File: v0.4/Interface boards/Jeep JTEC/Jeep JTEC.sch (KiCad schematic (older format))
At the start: 6 parts, among them J1 Conn_02x20_Counter_Clockwise

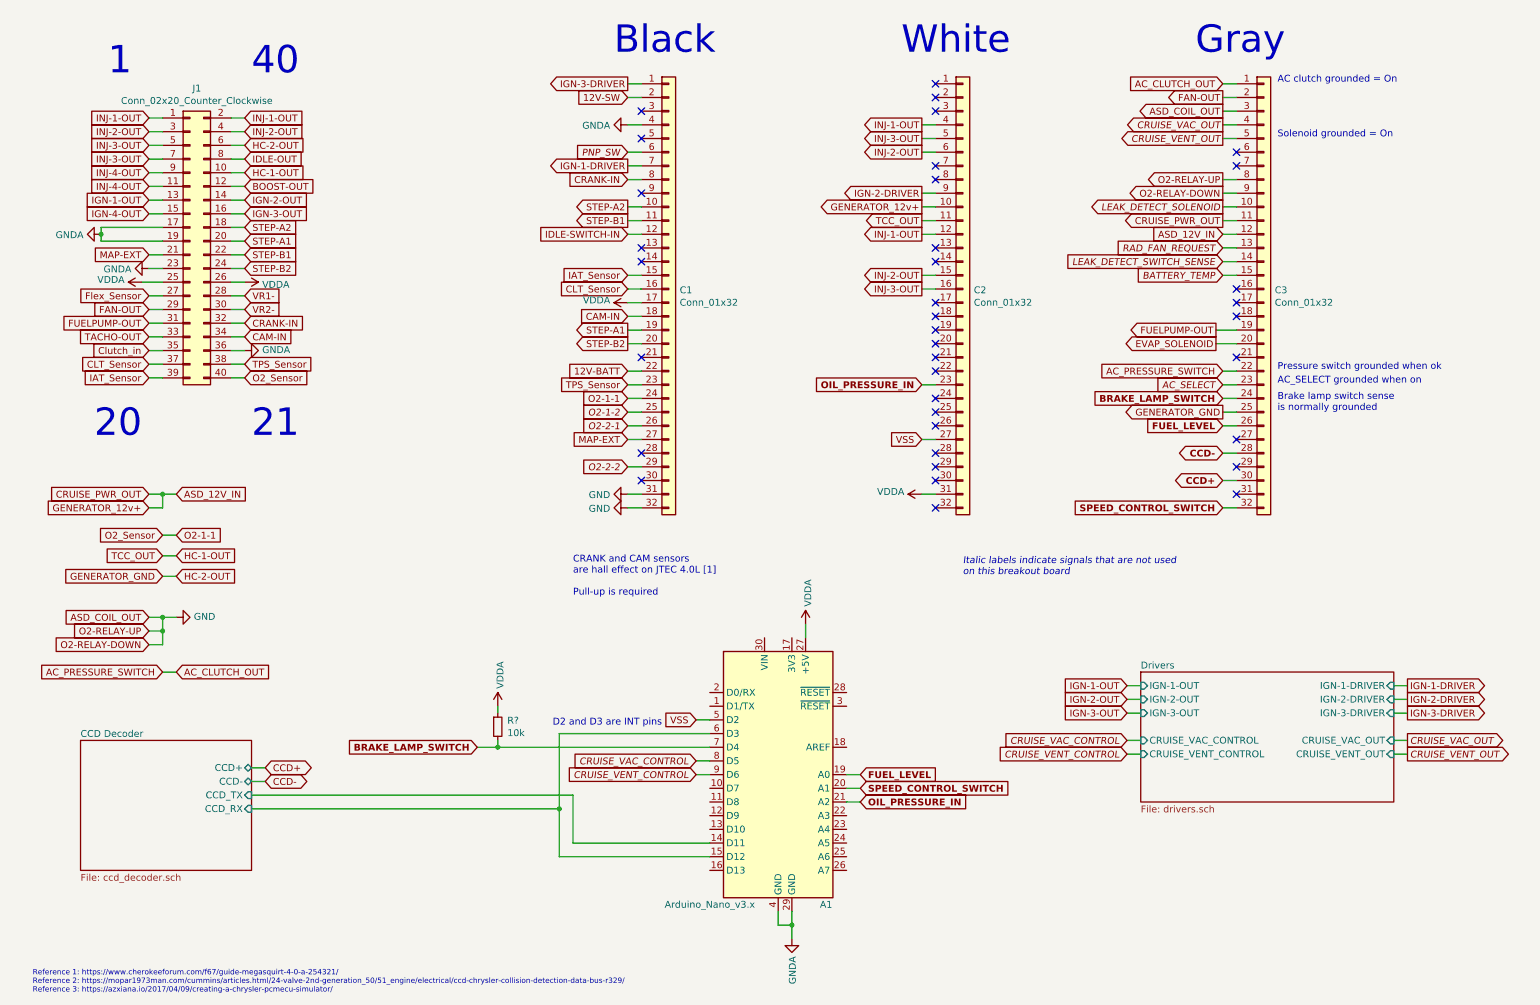
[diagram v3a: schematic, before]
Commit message: Add voltage sense circuit for alternator control
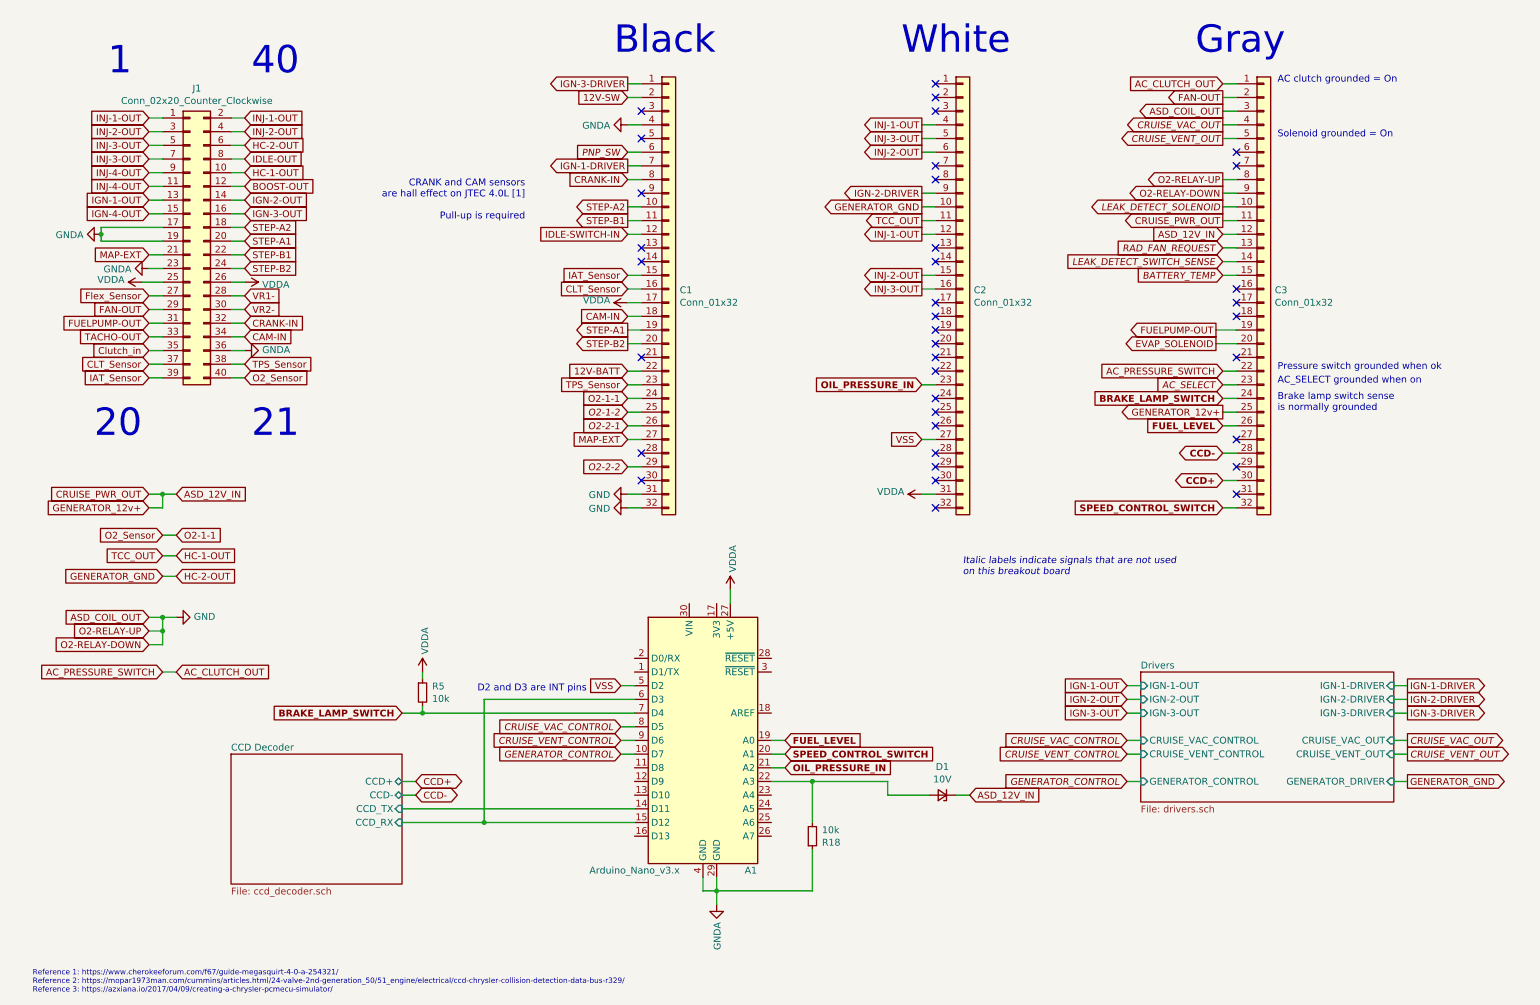
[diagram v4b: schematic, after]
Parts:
- added D1: 10V, Package_TO_SOT_SMD:SOT-23, symbol Misc:D_Zener_SOT-23
- added R18: 10k, Resistor_SMD:R_0805_2012Metric, symbol Device:R_Small
- R5: renamed from R?; footprint (none) -> Resistor_SMD:R_0805_2012Metric
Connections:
- net ASD_12V_IN: now also C3.25 (Pin_25), D1.3 (K); no longer C2.10 (Pin_10)
- net GENERATOR_GND: now also C2.10 (Pin_10); no longer C3.25 (Pin_25)
- net GNDA: now also R18.1
- net GENERATOR_CONTROL: now reaches A1.10 (D7)
- net at A1.22 (A3): now also D1.1 (A), R18.2
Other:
- moved on the sheet: A1, R5
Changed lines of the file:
@@
 Wire Wire Line
 	5000 1700 4900 1700
-Text Notes 4500 4750 0    50   ~ 0
+Text Notes 4150 2000 2    50   ~ 0
 CRANK and CAM sensors\nare hall effect on JTEC 4.0L [1]\n\nPull-up is required
 Text Notes 550  7650 0    39   ~ 0
@@
 Text GLabel 1600 4000 2    50   Input ~ 0
 ASD_12V_IN
-Text GLabel 7050 1900 0    50   Output ~ 0
+Text GLabel 9250 3400 0    50   Output ~ 0
 GENERATOR_12v+
 Wire Wire Line
@@
 Wire Wire Line
 	1400 5100 1500 5100
-Text GLabel 9250 3400 0    50   Output ~ 0
+Text GLabel 7050 1900 0    50   Output ~ 0
 GENERATOR_GND
 Wire Wire Line
@@
 L MCU_Module:Arduino_Nano_v3.x A1
 U 1 1 6153DDCF
-P 6000 6050
-F 0 "A1" H 6350 5100 50  0000 C CNN
-F 1 "Arduino_Nano_v3.x" H 5500 5100 50  0000 C CNN
-F 2 "Module:Arduino_Nano" H 6000 6050 50  0001 C CIN
-F 3 "http://www.mouser.com/pdfdocs/Gravitech_Arduino_Nano3_0.pdf" H 6000 6050 50  0001 C CNN
-	1    6000 6050
+P 5450 5800
+F 0 "A1" H 5800 4850 50  0000 C CNN
+F 1 "Arduino_Nano_v3.x" H 4950 4850 50  0000 C CNN
+F 2 "Module:Arduino_Nano" H 5450 5800 50  0001 C CIN
+F 3 "http://www.mouser.com/pdfdocs/Gravitech_Arduino_Nano3_0.pdf" H 5450 5800 50  0001 C CNN
+	1    5450 5800
 	1    0    0    -1
 $EndComp
-$Sheet
-S 900  5800 1250 950
-U 615FCF77
-F0 "CCD Decoder" 50
-F1 "ccd_decoder.sch" 50
-F2 "CCD-" B R 2150 6100 50
-F3 "CCD+" B R 2150 6000 50
-F4 "CCD_TX" I R 2150 6200 50
-F5 "CCD_RX" I R 2150 6300 50
-$EndSheet
-Wire Wire Line
-	5500 5750 4400 5750
-Wire Wire Line
-	4400 5750 4400 6300
-Wire Wire Line
-	4400 6300 2150 6300
-Wire Wire Line
-	5500 6650 4400 6650
-Wire Wire Line
-	5500 6550 4500 6550
-Wire Wire Line
-	4500 6550 4500 6200
-Wire Wire Line
-	4500 6200 2150 6200
+Wire Wire Line
+	4950 5500 3850 5500
+Wire Wire Line
+	4950 6400 3850 6400
 Text GLabel 9250 3700 0    50   BiDi ~ 10
 CCD-
 Text GLabel 9250 3900 0    50   BiDi ~ 10
 CCD+
-Text GLabel 2250 6000 2    50   BiDi ~ 0
-CCD+
-Wire Wire Line
-	2250 6000 2150 6000
-Text GLabel 2250 6100 2    50   BiDi ~ 0
-CCD-
-Wire Wire Line
-	2150 6100 2250 6100
-Wire Wire Line
-	4400 6300 4400 6650
-Connection ~ 4400 6300
 Text GLabel 9250 3500 0    50   Input ~ 10
 FUEL_LEVEL
-Text GLabel 6600 6050 2    50   Input ~ 10
+Text GLabel 6050 5800 2    50   Input ~ 10
 FUEL_LEVEL
 Wire Wire Line
-	6500 6050 6600 6050
-$Comp
-L power:VDDA #PWR?
+	5950 5800 6050 5800
+$Comp
+L power:VDDA #PWR017
 U 1 1 61616827
-P 6200 4950
-F 0 "#PWR?" H 6200 4800 50  0001 C CNN
-F 1 "VDDA" V 6218 5078 50  0000 L CNN
-F 2 "" H 6200 4950 50  0001 C CNN
-F 3 "" H 6200 4950 50  0001 C CNN
-	1    6200 4950
+P 5650 4700
+F 0 "#PWR017" H 5650 4550 50  0001 C CNN
+F 1 "VDDA" V 5668 4828 50  0000 L CNN
+F 2 "" H 5650 4700 50  0001 C CNN
+F 3 "" H 5650 4700 50  0001 C CNN
+	1    5650 4700
 	1    0    0    -1
 $EndComp
 Wire Wire Line
-	6200 5050 6200 4950
-$Comp
-L power:GNDA #PWR?
+	5650 4800 5650 4700
+$Comp
+L power:GNDA #PWR016
 U 1 1 6161D4CA
-P 6100 7250
-F 0 "#PWR?" H 6100 7000 50  0001 C CNN
-F 1 "GNDA" V 6105 7122 50  0000 R CNN
-F 2 "" H 6100 7250 50  0001 C CNN
-F 3 "" H 6100 7250 50  0001 C CNN
-	1    6100 7250
+P 5550 7000
+F 0 "#PWR016" H 5550 6750 50  0001 C CNN
+F 1 "GNDA" V 5555 6872 50  0000 R CNN
+F 2 "" H 5550 7000 50  0001 C CNN
+F 3 "" H 5550 7000 50  0001 C CNN
+	1    5550 7000
 	1    0    0    -1
 $EndComp
 Wire Wire Line
-	6100 7150 6100 7050
-Wire Wire Line
-	6100 7150 6000 7150
-Wire Wire Line
-	6000 7150 6000 7050
-Connection ~ 6100 7150
-Wire Wire Line
-	6100 7250 6100 7150
-Wire Wire Line
-	6600 6150 6500 6150
+	5550 6900 5550 6800
+Wire Wire Line
+	5550 6900 5450 6900
+Wire Wire Line
+	5450 6900 5450 6800
+Connection ~ 5550 6900
+Wire Wire Line
+	5550 7000 5550 6900
+Wire Wire Line
+	6050 5900 5950 5900
 Text GLabel 9250 4100 0    50   Input ~ 10
 SPEED_CONTROL_SWITCH
-Text GLabel 6600 6150 2    50   Input ~ 10
+Text GLabel 6050 5900 2    50   Input ~ 10
 SPEED_CONTROL_SWITCH
 Text GLabel 7050 3200 0    50   Input ~ 10
 OIL_PRESSURE_IN
-Text GLabel 6600 6250 2    50   Input ~ 10
+Text GLabel 6050 6000 2    50   Input ~ 10
 OIL_PRESSURE_IN
 Wire Wire Line
-	6600 6250 6500 6250
+	6050 6000 5950 6000
 Text GLabel 7050 3600 0    50   Input ~ 0
 VSS
-Text GLabel 5400 5650 0    50   Input ~ 0
+Text GLabel 4850 5400 0    50   Input ~ 0
 VSS
 Wire Wire Line
-	5400 5650 5500 5650
-Text Notes 5150 5700 2    50   ~ 0
+	4850 5400 4950 5400
+Text Notes 4600 5450 2    50   ~ 0
 D2 and D3 are INT pins
 Text GLabel 7050 1300 0    50   Output ~ 0
@@
 Text GLabel 9250 3300 0    50   Input ~ 10
 BRAKE_LAMP_SWITCH
-Text GLabel 3800 5850 0    50   Input ~ 10
+Text GLabel 3250 5600 0    50   Input ~ 10
 BRAKE_LAMP_SWITCH
 $Comp
 L Device:R_Small R?
 U 1 1 6173A1FE
-P 3950 5700
+P 3400 5450
 AR Path="/615FCF77/6173A1FE" Ref="R?"  Part="1"
-AR Path="/6173A1FE" Ref="R?"  Part="1"
-F 0 "R?" H 4020 5746 50  0000 L CNN
-F 1 "10k" H 4020 5655 50  0000 L CNN
-F 2 "" V 3880 5700 50  0001 C CNN
-F 3 "~" H 3950 5700 50  0001 C CNN
-	1    3950 5700
+AR Path="/6173A1FE" Ref="R5"  Part="1"
+F 0 "R5" H 3470 5496 50  0000 L CNN
+F 1 "10k" H 3470 5405 50  0000 L CNN
+F 2 "Resistor_SMD:R_0805_2012Metric" V 3330 5450 50  0001 C CNN
+F 3 "~" H 3400 5450 50  0001 C CNN
+	1    3400 5450
 	1    0    0    -1
 $EndComp
 Wire Wire Line
-	3950 5550 3950 5600
-Wire Wire Line
-	3950 5800 3950 5850
-Wire Wire Line
-	5500 5850 3950 5850
-Connection ~ 3950 5850
-Wire Wire Line
-	3950 5850 3800 5850
-$Comp
-L power:VDDA #PWR?
+	3400 5300 3400 5350
+Wire Wire Line
+	3400 5550 3400 5600
+Wire Wire Line
+	4950 5600 3400 5600
+Connection ~ 3400 5600
+Wire Wire Line
+	3400 5600 3250 5600
+$Comp
+L power:VDDA #PWR015
 U 1 1 617EB87A
-P 3950 5550
-F 0 "#PWR?" H 3950 5400 50  0001 C CNN
-F 1 "VDDA" V 3968 5678 50  0000 L CNN
-F 2 "" H 3950 5550 50  0001 C CNN
-F 3 "" H 3950 5550 50  0001 C CNN
-	1    3950 5550
+P 3400 5300
+F 0 "#PWR015" H 3400 5150 50  0001 C CNN
+F 1 "VDDA" V 3418 5428 50  0000 L CNN
+F 2 "" H 3400 5300 50  0001 C CNN
+F 3 "" H 3400 5300 50  0001 C CNN
+	1    3400 5300
 	1    0    0    -1
 $EndComp
@@
 Wire Wire Line
 	10600 5900 10500 5900
-Text GLabel 5400 5950 0    50   Input Italic 0
+Text GLabel 4850 5700 0    50   Input Italic 0
 CRUISE_VAC_CONTROL
 Wire Wire Line
-	5400 5950 5500 5950
-Text GLabel 5400 6050 0    50   Input Italic 0
+	4850 5700 4950 5700
+Text GLabel 4850 5800 0    50   Input Italic 0
 CRUISE_VENT_CONTROL
 Wire Wire Line
-	5400 6050 5500 6050
+	4850 5800 4950 5800
 Text GLabel 8550 5800 0    50   Input Italic 0
 CRUISE_VAC_CONTROL
@@
 F10 "CRUISE_VENT_CONTROL" I L 8650 5900 50
 F11 "CRUISE_VENT_OUT" I R 10500 5900 50
+F12 "GENERATOR_CONTROL" I L 8650 6100 50
+F13 "GENERATOR_DRIVER" I R 10500 6100 50
 $EndSheet
+Text GLabel 10600 6100 2    50   Output ~ 0
+GENERATOR_GND
+Wire Wire Line
+	10600 6100 10500 6100
+Text GLabel 4850 5900 0    50   Input Italic 0
+GENERATOR_CONTROL
+Wire Wire Line
+	4850 5900 4950 5900
+Text GLabel 8550 6100 0    50   Input Italic 0
+GENERATOR_CONTROL
+Wire Wire Line
+	8550 6100 8650 6100
+$Comp
+L Device:R_Small R?
+U 1 1 618ADDF1
+P 6250 6500
+AR Path="/615FCF77/618ADDF1" Ref="R?"  Part="1"
+AR Path="/618ADDF1" Ref="R18"  Part="1"
+F 0 "R18" H 6320 6546 50  0000 L CNN
+F 1 "10k" H 6320 6455 50  0000 L CNN
+F 2 "Resistor_SMD:R_0805_2012Metric" V 6180 6500 50  0001 C CNN
+F 3 "~" H 6250 6500 50  0001 C CNN
+	1    6250 6500
+	1    0    0    1
+$EndComp
+Wire Wire Line
+	6250 6100 6250 6400
+Wire Wire Line
+	6250 6600 6250 6900
+Wire Wire Line
+	6250 6900 5550 6900
+Wire Wire Line
+	6250 6100 5950 6100
+Connection ~ 6250 6100
+Wire Wire Line
+	3250 6200 3350 6200
+Text GLabel 3350 6200 2    50   BiDi ~ 0
+CCD-
+Wire Wire Line
+	3350 6100 3250 6100
+Text GLabel 3350 6100 2    50   BiDi ~ 0
+CCD+
+$Sheet
+S 2000 5900 1250 950
+U 615FCF77
+F0 "CCD Decoder" 50
+F1 "ccd_decoder.sch" 50
+F2 "CCD-" B R 3250 6200 50
+F3 "CCD+" B R 3250 6100 50
+F4 "CCD_TX" I R 3250 6300 50
+F5 "CCD_RX" I R 3250 6400 50
+$EndSheet
+Wire Wire Line
+	3850 5500 3850 6400
+Wire Wire Line
+	3850 6400 3250 6400
+Connection ~ 3850 6400
+Wire Wire Line
+	3250 6300 4950 6300
+$Comp
+L Misc:D_Zener_SOT-23 D1
+U 1 1 618B7D29
+P 7200 6200
+F 0 "D1" H 7200 5993 50  0000 C CNN
+F 1 "10V" H 7200 6084 50  0000 C CNN
+F 2 "Package_TO_SOT_SMD:SOT-23" V 7200 6200 50  0001 C CNN
+F 3 "~" V 7200 6200 50  0001 C CNN
+F 4 "BZX84-C10,215" H 7200 6200 50  0001 C CNN "Manufacturer"
+F 5 "Nexperia USA Inc." H 7200 6200 50  0001 C CNN "Manufacturer#"
+F 6 "1727-2935-1-ND" H 7200 6200 50  0001 C CNN "digikey#"
+	1    7200 6200
+	-1   0    0    1
+$EndComp
+Wire Wire Line
+	7300 6200 7400 6200
+Wire Wire Line
+	6800 6100 6800 6200
+Wire Wire Line
+	6800 6200 7100 6200
+Wire Wire Line
+	6250 6100 6800 6100
+Text GLabel 7400 6200 2    50   Input ~ 0
+ASD_12V_IN
 $EndSCHEMATC

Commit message: Route PCB for JTEC breakout
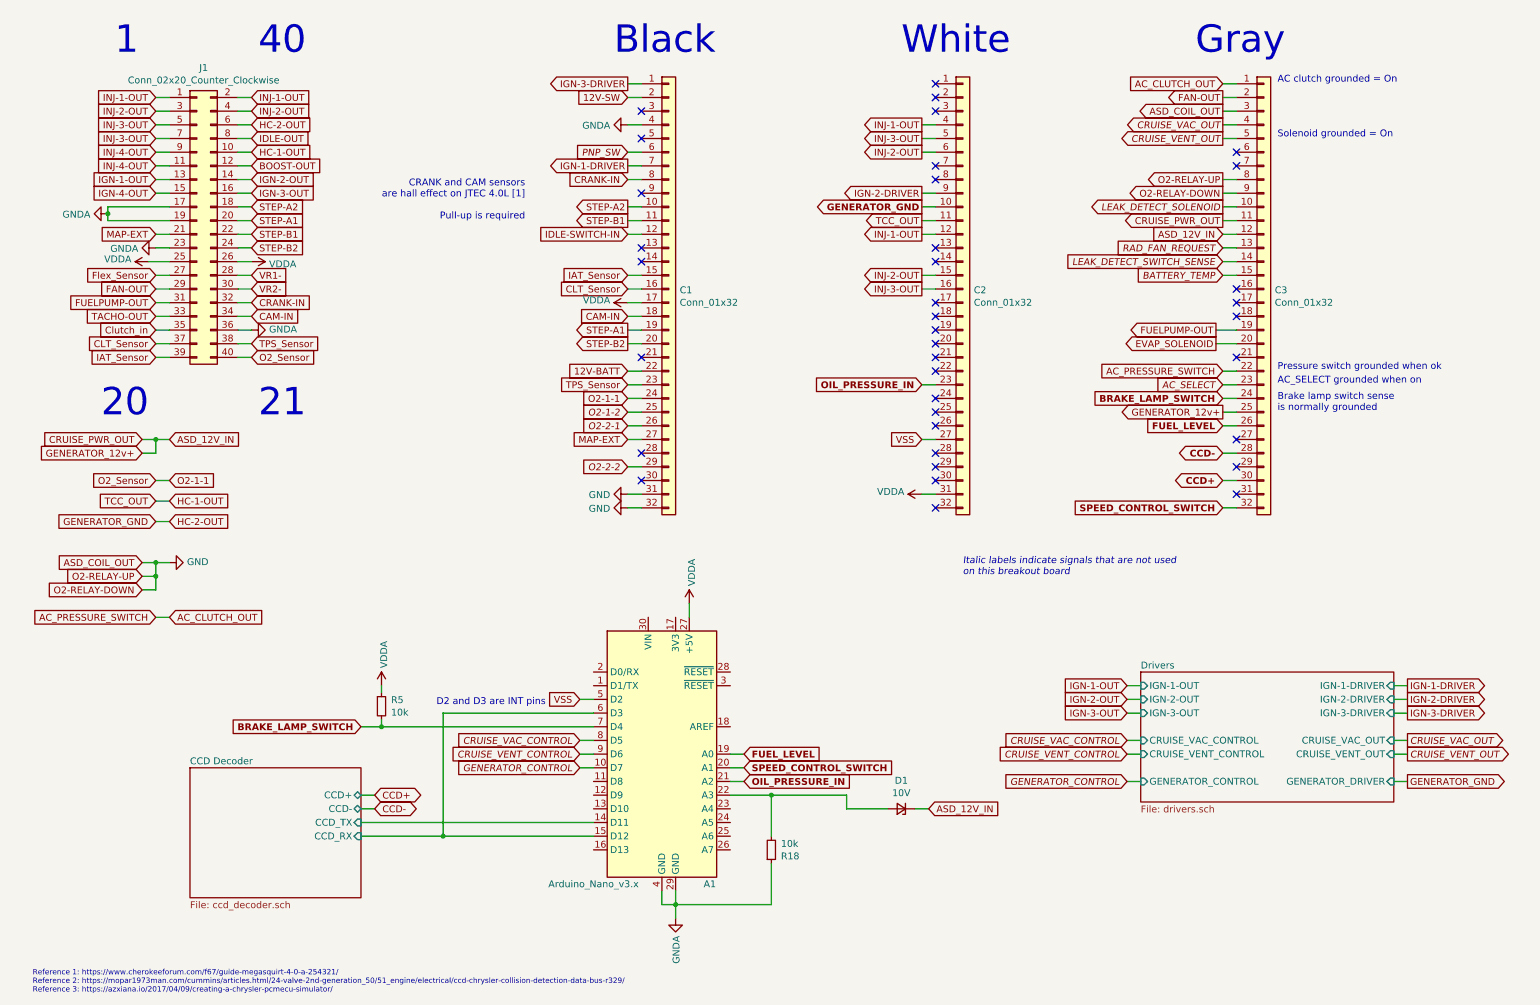
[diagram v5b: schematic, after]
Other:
- moved on the sheet: A1, D1, J1, R18, R5

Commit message: Add BOM items for jellybean parts
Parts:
- J1: Manufacturer (none) -> 302-S401; Manufacturer# (none) -> On Shore Technology Inc.; digikey# (none) -> ED10529-ND
- R18, R5: Manufacturer (none) -> Yageo; Manufacturer# (none) -> RC0805FR-0710KL
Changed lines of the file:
@@
 EESchema Schematic File Version 4
+LIBS:Jeep JTEC-cache
 EELAYER 30 0
 EELAYER END
@@
 F 2 "Connector_IDC:IDC-Header_2x20_P2.54mm_Vertical" H 1750 2000 50  0001 C CNN
 F 3 "~" H 1750 2000 50  0001 C CNN
+F 4 "302-S401" H 1750 2000 50  0001 C CNN "Manufacturer"
+F 5 "	On Shore Technology Inc." H 1750 2000 50  0001 C CNN "Manufacturer#"
+F 6 "ED10529-ND" H 1750 2000 50  0001 C CNN "digikey#"
 	1    1750 2000
 	1    0    0    -1
@@
 F 2 "Resistor_SMD:R_0805_2012Metric" V 3030 5550 50  0001 C CNN
 F 3 "~" H 3100 5550 50  0001 C CNN
+F 4 "Yageo" H 3100 5550 50  0001 C CNN "Manufacturer"
+F 5 "RC0805FR-0710KL" H 3100 5550 50  0001 C CNN "Manufacturer#"
 	1    3100 5550
 	1    0    0    -1
@@
 F 2 "Resistor_SMD:R_0805_2012Metric" V 5880 6600 50  0001 C CNN
 F 3 "~" H 5950 6600 50  0001 C CNN
+F 4 "Yageo" H 5950 6600 50  0001 C CNN "Manufacturer"
+F 5 "RC0805FR-0710KL" H 5950 6600 50  0001 C CNN "Manufacturer#"
 	1    5950 6600
 	1    0    0    1
